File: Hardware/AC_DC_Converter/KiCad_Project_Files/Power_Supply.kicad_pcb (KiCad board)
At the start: 2 copper layers, 100 x 50 mm, 106 parts, among them J2 Conn_01x01, J3 Conn_01x01, J4 Screw_Terminal_01x02, J5 USB_C_Receptacle_USB2.0, Q1 FDN335N, Q2 FDN335N, Q3 FDN335N, SW1 UP, SW2 DW, SW3 V_I_SEL, SW4 O_EN, U1 MIC5205-5.0YM5, U10 SSD1306_0.96in, U11 LM358, U2 ATmega328PB-AU, U3 TPS54531DDAR, U4 LM358, U5 INA138, U6 MCP4023-103ECH, U7 CH340E, U8 MIC5205-3.3YM5, U9 PCA9306, Y1 16MHz

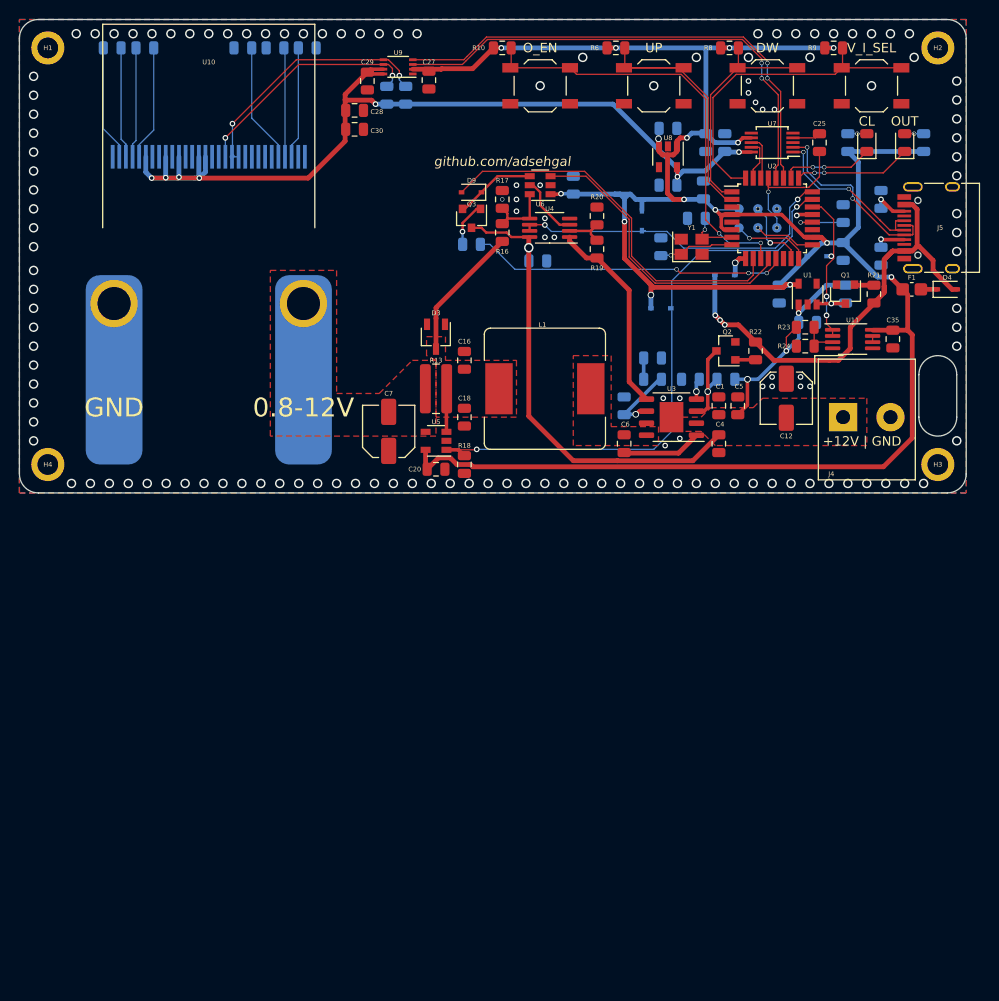
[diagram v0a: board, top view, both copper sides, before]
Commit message: ac dc converter schem complete
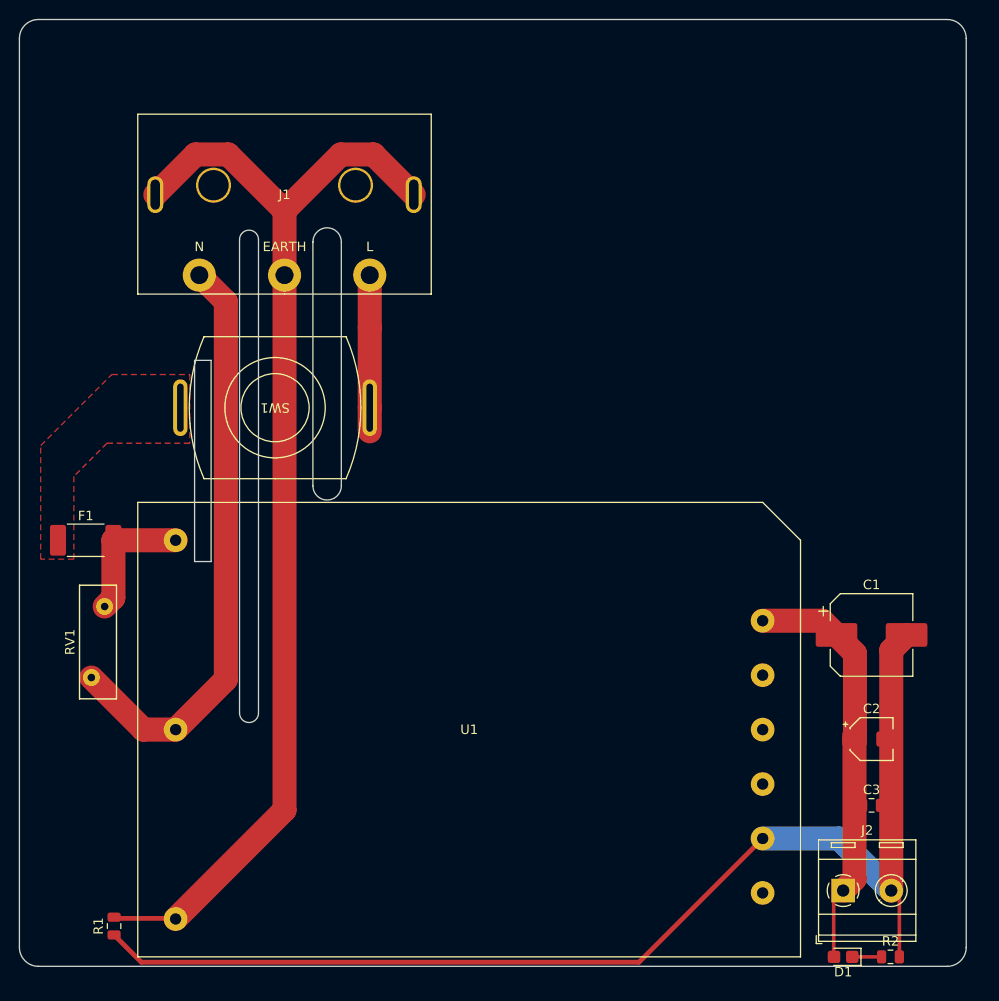
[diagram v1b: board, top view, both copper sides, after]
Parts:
- removed C10, C19, C20, C21, C22, C23, C24, C25, C27, C28, C35, C6, C9: 100nF, Capacitor_SMD:C_0805_2012Metric
- removed C11, C26, C29, C30, C31, C33: 1µF, Capacitor_SMD:C_0805_2012Metric
- removed C12, C7: 10uF, Capacitor_SMD:C_Elec_5x5.4
- removed C13: 2.2nF, Capacitor_SMD:C_0805_2012Metric
- removed C14, C15, C17: 22pF, Capacitor_SMD:C_0805_2012Metric
- removed C16, C18, C32, C4, C5: 4.7µF, Capacitor_SMD:C_0805_2012Metric
- removed C34: 2.2µF, Capacitor_SMD:C_0805_2012Metric
- removed C8: 10nF, Capacitor_SMD:C_0805_2012Metric
- removed D2: OUT, LED_SMD:LED_0805_2012Metric
- removed D3: BAT1000, Package_TO_SOT_SMD:TSOT-23
- removed D4, D5, D6, D7, D8, D9: CUS10S30, Diode_SMD:D_SOD-323
- removed H1, H2, H3, H4: MountingHole_Pad, MountingHole:MountingHole_2.2mm_M2_ISO7380_Pad
- removed the J2 at (42.0, 42.0)
- removed J3: Conn_01x01, Binding_Post:Binding_Post
- removed J5: USB_C_Receptacle_USB2.0, Connector_USB:USB_C_Receptacle_HRO_TYPE-C-31-M-12
- removed L1: 4.7µH, Inductor_SMD:L_Bourns_SRR1260
- removed Q1, Q2, Q3: FDN335N, Package_TO_SOT_SMD:SOT-23
- removed R10, R12, R17, R20, R24, R3, R6, R8, R9: 10K, Resistor_SMD:R_0805_2012Metric
- removed R11, R4: 5.1K, Resistor_SMD:R_0805_2012Metric
- removed R13: 0.01R, Resistor_SMD:R_1020_2550Metric
- removed R14, R5: 2.2K, Resistor_SMD:R_0805_2012Metric
- removed R15: 390K, Resistor_SMD:R_0805_2012Metric
- removed R16, R19, R23: 14K, Resistor_SMD:R_0805_2012Metric
- removed R18: 500K, Resistor_SMD:R_0805_2012Metric
- removed R21, R22, R25: 1K, Resistor_SMD:R_0805_2012Metric
- removed R7: 37.4K, Resistor_SMD:R_0805_2012Metric
- removed SW2: DW, Button_Switch_SMD:SW_SPST_TL3342
- removed SW3: V_I_SEL, Button_Switch_SMD:SW_SPST_TL3342
- removed SW4: O_EN, Button_Switch_SMD:SW_SPST_TL3342
- removed TP1, TP2, TP3, TP4, TP5, TP6: TestPoint, TestPoint:TestPoint_Pad_D1.0mm
- removed U10: SSD1306_0.96in, Custom_Displays:SSD1306_0.96in
- removed U11, U4: LM358, Package_SO:MSOP-8_3x3mm_P0.65mm
- removed U2: ATmega328PB-AU, Package_QFP:TQFP-32_7x7mm_P0.8mm
- removed U3: TPS54531DDAR, Package_SO:SOIC-8-1EP_3.9x4.9mm_P1.27mm_EP2.514x3.2mm
- removed U5: INA138, Package_TO_SOT_SMD:SOT-23-5
- removed U6: MCP4023-103ECH, Package_TO_SOT_SMD:SOT-23-6
- removed U7: CH340E, Package_SO:MSOP-10_3x3mm_P0.5mm
- removed U8: MIC5205-3.3YM5, Package_TO_SOT_SMD:SOT-23-5
- removed U9: PCA9306, Package_SO:VSSOP-8_2.3x2mm_P0.5mm
- removed Y1: 16MHz, Crystal:Crystal_SMD_SeikoEpson_TSX3225-4Pin_3.2x2.5mm
- added J1: IEC Conn, IEC_Conn:ACT3KD-03BT3B018, F.Cu at (40.0, 39.0)
- added RV1: ERZE10E471, Varistor:RV_Disc_D12mm_W3.9mm_P7.5mm, F.Cu at (21.0, 74.0)
- C1: value 10nF -> 220µF; footprint Capacitor_SMD:C_0805_2012Metric -> Capacitor_SMD:CP_Elec_8x10.5
- C2: value 100nF -> 1µF; footprint Capacitor_SMD:C_0805_2012Metric -> Capacitor_SMD:CP_Elec_4x5.4; moved to F.Cu
- C3: moved to F.Cu
- D1: value CL -> PWR; footprint LED_SMD:LED_0805_2012Metric -> LED_SMD:LED_0805_2012Metric_Castellated
- F1: value MF-PSMF020X-2 -> 0443002.DR; footprint Fuse:Fuse_0805_2012Metric_Castellated -> Fuse:Fuse_2512_6332Metric_Castellated
- J2: renamed from J4; footprint TerminalBlock_Altech:Altech_AK300_1x02_P5.00mm_45-Degree -> TerminalBlock_RND:TerminalBlock_RND_205-00287_1x02_P5.08mm_Horizontal
- R1: value 330R -> 100R; moved to F.Cu
- R2: value 330R -> 2K; moved to F.Cu
- SW1: value UP -> ON/OFF; footprint Button_Switch_SMD:SW_SPST_TL3342 -> BPT_Switch:BPT
- U1: value MIC5205-5.0YM5 -> TAS40-12-W; footprint Package_TO_SOT_SMD:SOT-23-5 -> TAS40-12-W:TAS40-12-W
- moved R1 113.4 mm to (22.0, 107.8), turned to 90 degrees
- moved F1 91.2 mm to (19.0, 67.0), turned to 0 degrees
- moved R2 86.1 mm to (104.0, 111.0), turned to 0 degrees
- moved D1 86.0 mm to (99.0, 111.0), turned to 180 degrees
- moved U1 58.3 mm to (59.5, 87.0), turned to 0 degrees
- moved C2 55.6 mm to (102.0, 88.0), turned to 0 degrees
- moved SW1 52.5 mm to (39.0, 53.0), turned to 180 degrees
- moved C3 51.4 mm to (102.0, 95.0), turned to 0 degrees
- moved G*** 50.0 mm to (65.0, 74.0) (x2)
- moved J2 50.0 mm to (99.0, 104.0)
- moved C1 29.1 mm to (102.0, 77.0), turned to 0 degrees
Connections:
- C1 pad 1: GND -> Net-(C1-Pad1)
- C1 pad 2: +VSW -> GND
- C2 pad 1: GND -> Net-(C1-Pad1)
- C2 pad 2: Net-(C2-Pad2) -> GND
- C3 pad 1: GND -> Net-(C1-Pad1)
- C3 pad 2: +VSW -> GND
- D1 pad 2: Net-(D1-Pad2) -> Net-(C1-Pad1)
- F1 pad 1: Net-(D4-Pad1) -> Net-(F1-Pad1)
- F1 pad 2: +5V -> Net-(F1-Pad2)
- J2 pad 1: +VSW -> Net-(C1-Pad1)
- R1 pad 1: Net-(D1-Pad2) -> GND
- R1 pad 2: +5V -> Net-(J1-Pad3)
- R2 pad 1: Net-(D2-Pad2) -> Net-(D1-Pad1)
- R2 pad 2: +5V -> GND
- SW1 pad 1: /SW1 -> Net-(J1-Pad1)
- SW1 pad 2: GND -> Net-(F1-Pad1)
- U1 pad 1: +VSW -> Net-(F1-Pad2)
- U1 pad 2: GND -> Net-(J1-Pad2)
- U1 pad 3: Net-(Q1-Pad3) -> Net-(J1-Pad3)
- U1 pad 5: +5V -> GND
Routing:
- net +5V: track 270.3 -> 0.00 mm, vias 15 -> 0
- net GND: track 1.69 -> 126.0 mm, vias 140 -> 0
- net Net-(J1-Pad3): track 0.00 -> 121.8 mm
- net +3V3: track 100.6 -> 0.00 mm, vias 7 -> 0
- net +VSW: track 75.5 -> 0.00 mm, vias 4 -> 0
- net /I_SENSE: track 62.8 -> 0.00 mm, vias 2 -> 0
- net Net-(J1-Pad2): track 0.00 -> 62.5 mm
- net /SDA0: track 52.6 -> 0.00 mm, vias 2 -> 0
- net /SCL0: track 52.2 -> 0.00 mm, vias 2 -> 0
- net /REG_EN: track 49.9 -> 0.00 mm, vias 3 -> 0
- net /SW4: track 45.4 -> 0.00 mm, vias 2 -> 0
- net Net-(C1-Pad1): track 0.00 -> 44.2 mm
- net /~POT_CS: track 40.8 -> 0.00 mm
- net /V_SENSE: track 35.8 -> 0.00 mm, vias 2 -> 0
- net /SW3: track 34.2 -> 0.00 mm
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- added copper zone on F.Cu, net Net-(F1-Pad1)
- removed copper zone on F.Cu, net +VSW
- removed copper zone on B.Cu, net GND
- removed copper zone on F.Cu, net GND
- removed copper zone on F.Cu, net Net-(C16-Pad2)
- removed copper zone on F.Cu, net Net-(C6-Pad2)
- removed copper zone on F.Cu, net VDC
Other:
- board size 100 x 50 mm -> 100 x 100 mm
- board text removed: "+12V | GND"
- board text removed: "0.8-12V"
- board text removed: "Bench Top PSU V1.0"
- board text removed: "GND"
- board text removed: "GND | +12V"
- board text removed: "github.com/adsehgal"

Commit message: ac-dc layout compelte
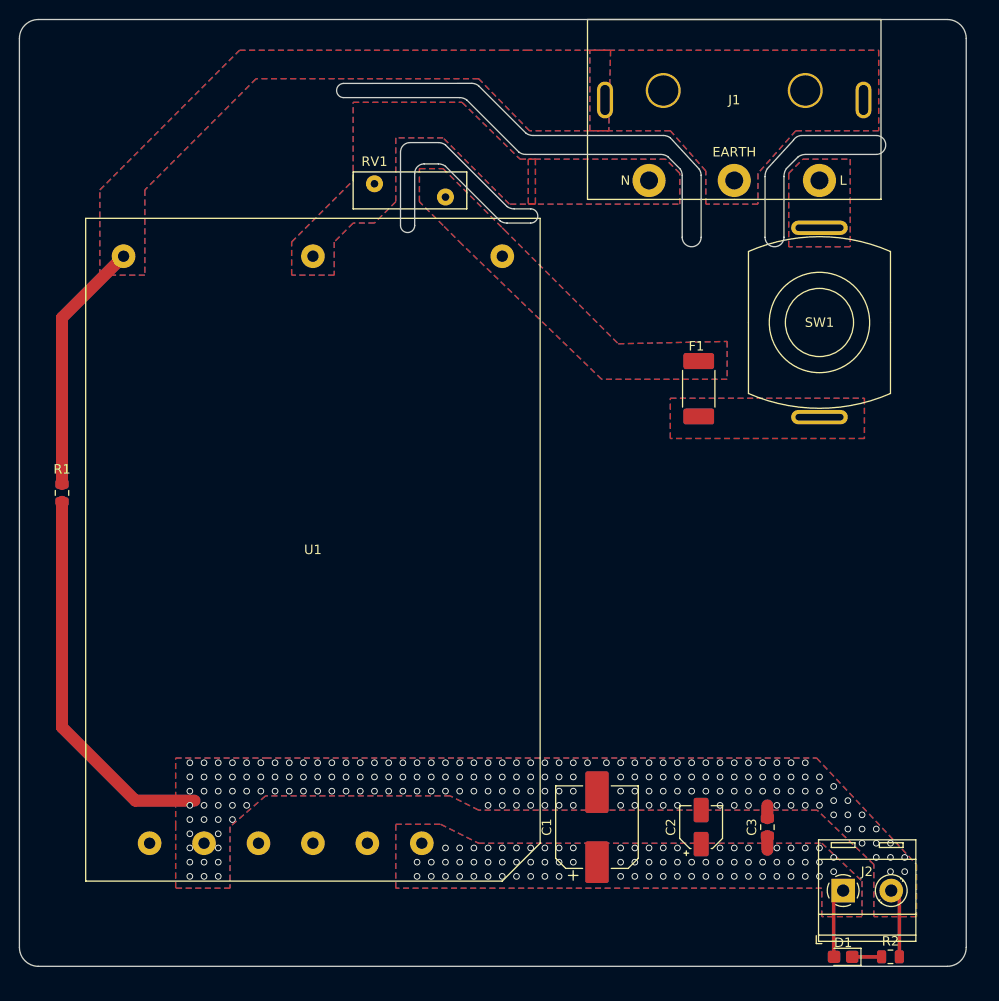
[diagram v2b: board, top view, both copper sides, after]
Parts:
- moved F1 66.7 mm to (83.8, 51.0), turned to 90 degrees
- moved SW1 58.2 mm to (96.5, 44.0), turned to -90 degrees
- moved RV1 56.3 mm to (57.0, 30.8), turned to 180 degrees
- moved J1 48.5 mm to (87.5, 29.0)
- moved R1 46.1 mm to (16.5, 62.0)
- moved C1 35.4 mm to (73.0, 97.3), turned to 90 degrees
- moved U1 25.2 mm to (43.0, 68.0), turned to -90 degrees
- moved C2 20.3 mm to (84.0, 97.3), turned to 90 degrees
- moved C3 11.2 mm to (91.0, 97.3), turned to 90 degrees
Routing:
- net Net-(J1-Pad3): track 121.8 -> 26.8 mm
- net GND: track 126.0 -> 48.5 mm, vias 0 -> 185
- net Net-(J1-Pad2): track 62.5 -> 0.00 mm
- net Net-(C1-Pad1): track 44.2 -> 7.48 mm, vias 0 -> 77
- net Net-(J1-Pad1): track 16.5 -> 0.00 mm
- net Net-(F1-Pad2): track 14.0 -> 0.00 mm
- added copper zone on B.Cu, net GND
- added copper zone on F.Cu, net GND
- added copper zone on B.Cu, net Net-(C1-Pad1)
- added copper zone on F.Cu, net Net-(C1-Pad1)
- added copper zone on B.Cu, net Net-(F1-Pad1)
- added copper zone on B.Cu, net Net-(F1-Pad2)
- added copper zone on F.Cu, net Net-(F1-Pad2)
- added copper zone on B.Cu, net Net-(J1-Pad1)
- added copper zone on F.Cu, net Net-(J1-Pad1)
- added copper zone on B.Cu, net Net-(J1-Pad2)
- added copper zone on F.Cu, net Net-(J1-Pad2)
- added copper zone on B.Cu, net Net-(J1-Pad3)
- added copper zone on F.Cu, net Net-(J1-Pad3)
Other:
- outline, holes or cut-outs redrawn

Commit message: ac-dc layout complete and added 3d models
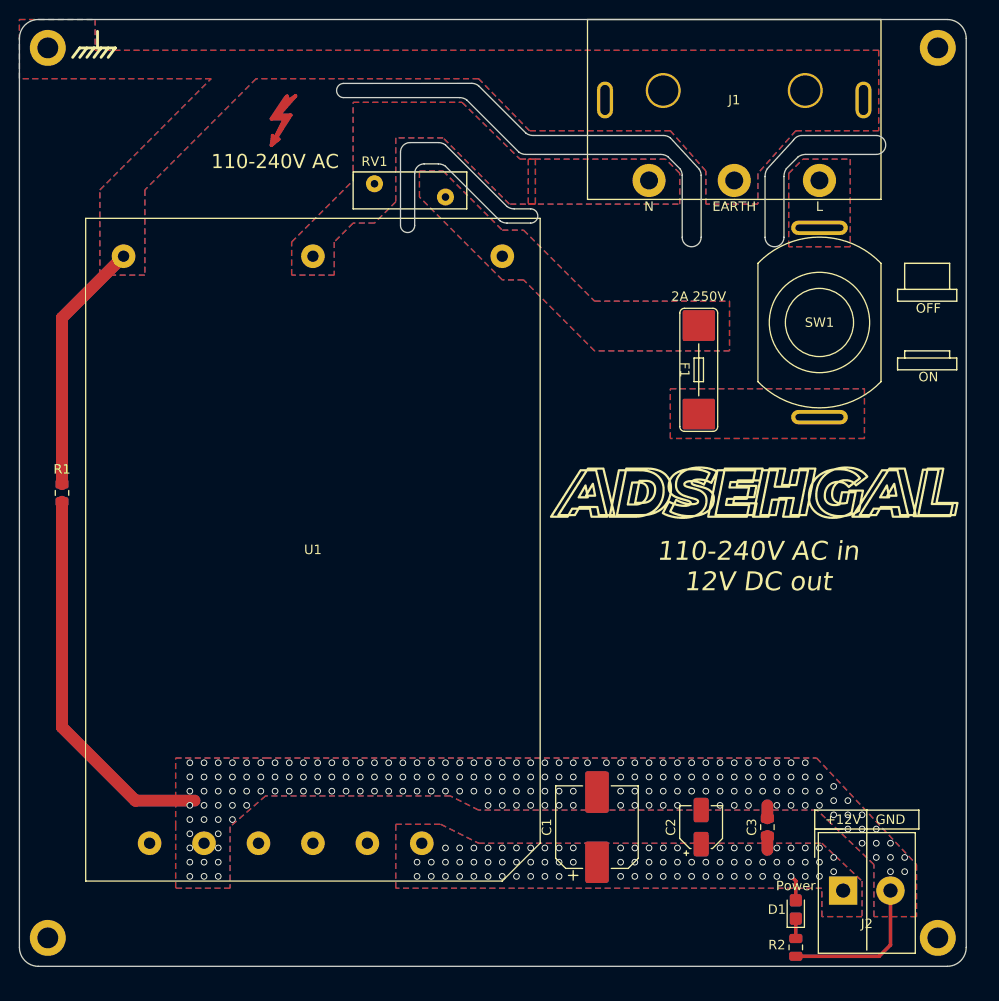
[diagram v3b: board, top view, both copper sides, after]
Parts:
- removed the G*** at (65.0, 74.0) (x2)
- added G***: LOGO, LOGO, F.Cu at (89.8, 62.0)
- added G***: LOGO, LOGO, B.Cu at (89.8, 62.0)
- added H1: MountingHole, MountingHole:MountingHole_2.2mm_M2_DIN965_Pad, F.Cu at (109.0, 109.0)
- added H2: Earth, MountingHole:MountingHole_2.2mm_M2_DIN965_Pad, F.Cu at (15.0, 15.0)
- added H3: MountingHole, MountingHole:MountingHole_2.2mm_M2_DIN965_Pad, F.Cu at (109.0, 15.0)
- added H4: MountingHole, MountingHole:MountingHole_2.2mm_M2_DIN965_Pad, F.Cu at (15.0, 109.0)
- added REF**: Symbol_Highvoltage_Type1_CopperTop_Small, Symbol:Symbol_Highvoltage_Type1_CopperTop_Small, F.Cu at (39.0, 23.2)
- F1: footprint Fuse:Fuse_2512_6332Metric_Castellated -> Custom_Fuses:LittleFuse-0443002
- J2: footprint TerminalBlock_RND:TerminalBlock_RND_205-00287_1x02_P5.08mm_Horizontal -> TerminalBlock_Altech:Altech_AK300_1x02_P5.00mm_45-Degree
- moved R2 10.0 mm to (94.0, 110.0), turned to -90 degrees
- moved D1 7.07 mm to (94.0, 106.0), turned to 90 degrees
- moved F1 2.00 mm to (83.8, 49.0), turned to -90 degrees
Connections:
- net Net-(J1-Pad3) renamed Earth
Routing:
- net GND: track 48.5 -> 58.6 mm
- net Net-(C1-Pad1): track 7.48 -> 4.21 mm
- net Net-(D1-Pad1): track 3.10 -> 2.10 mm
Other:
- board text added: "+12V"
- board text added: "110-240V AC"
- board text added: "110-240V AC in 12V DC out"
- board text added: "2A 250V"
- board text added: "GND"
- board text added: "OFF"
- board text added: "ON"
- board text added: "Power"
